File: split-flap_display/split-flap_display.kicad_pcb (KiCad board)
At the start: 2 copper layers, 190 x 133.9 mm, 5 parts, among them U1 MIC59P60, U2 ESP-12, U3 MIC59P60, U4 MIC59P60, U5 74LS597

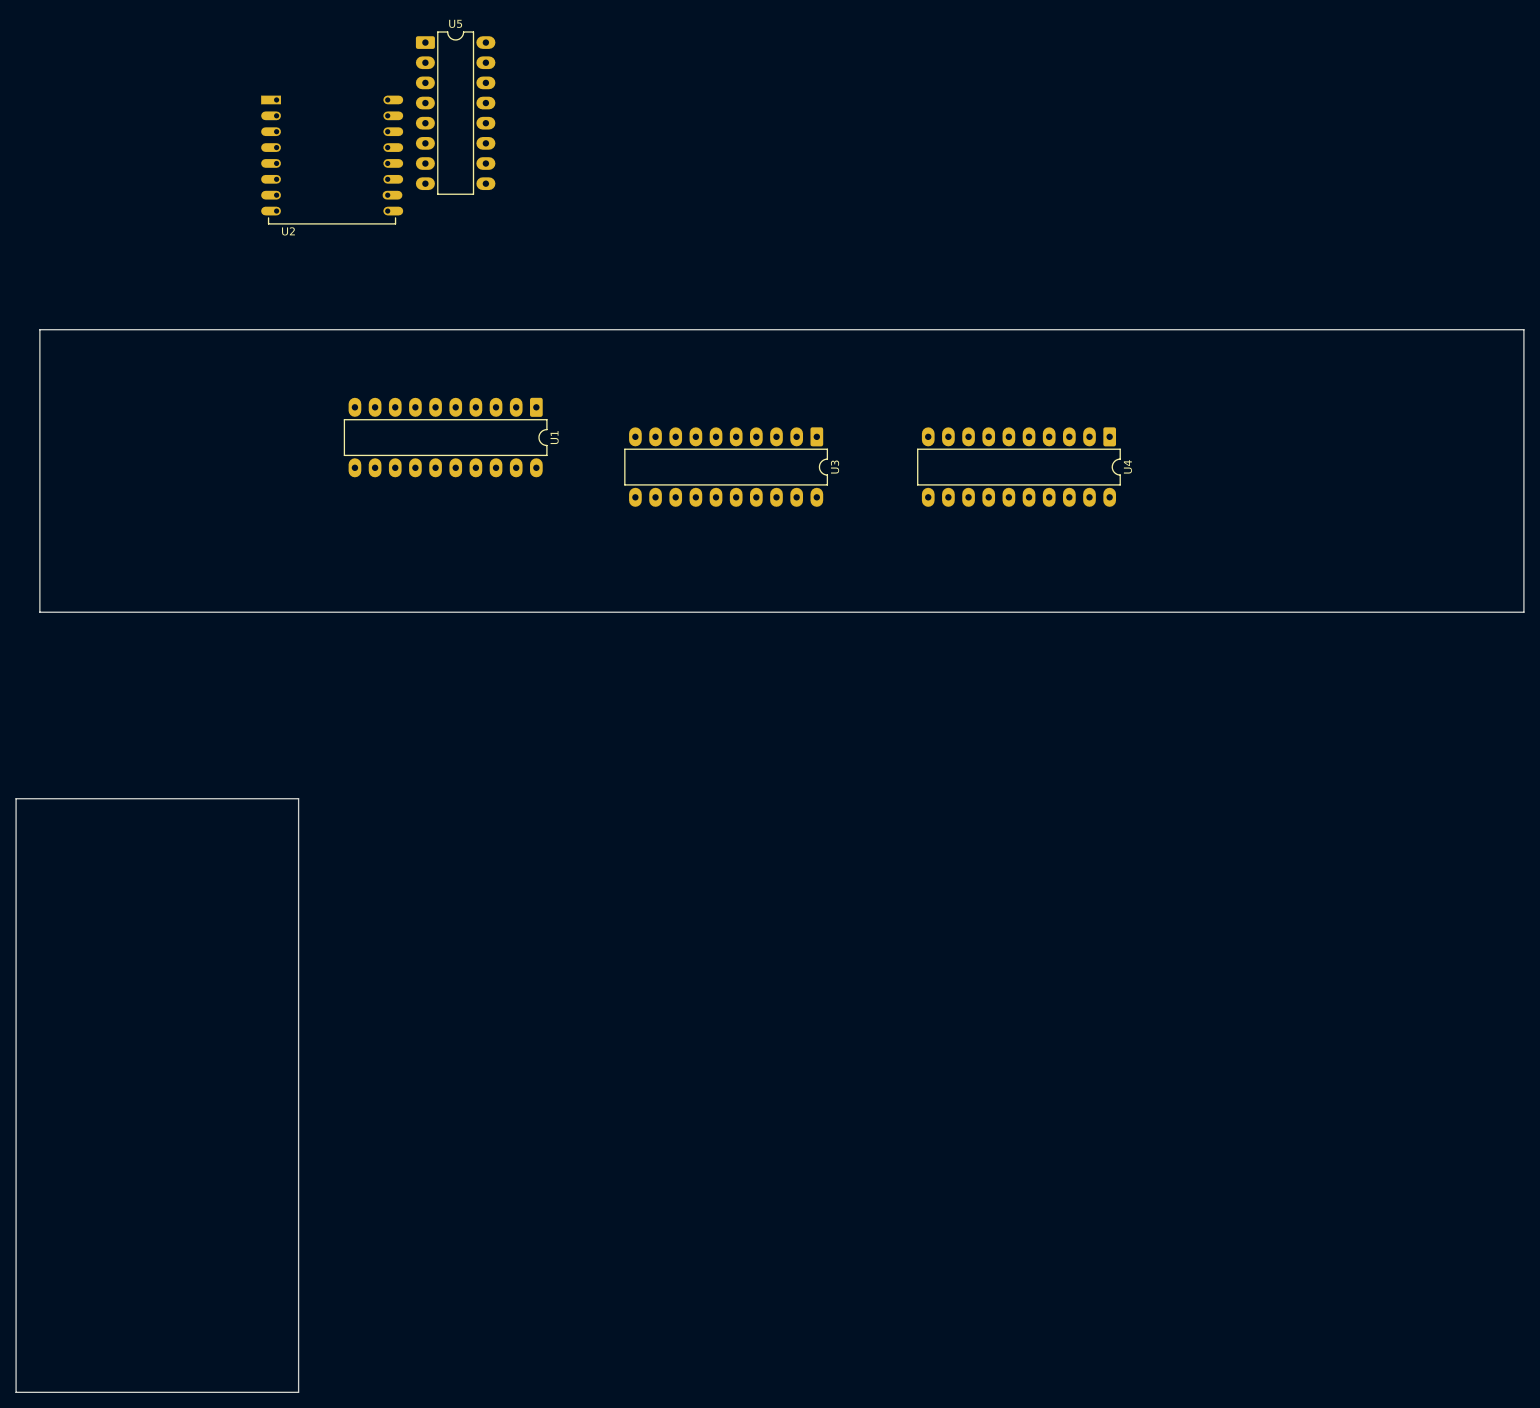
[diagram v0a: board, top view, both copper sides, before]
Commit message: added split flap source files & assembly
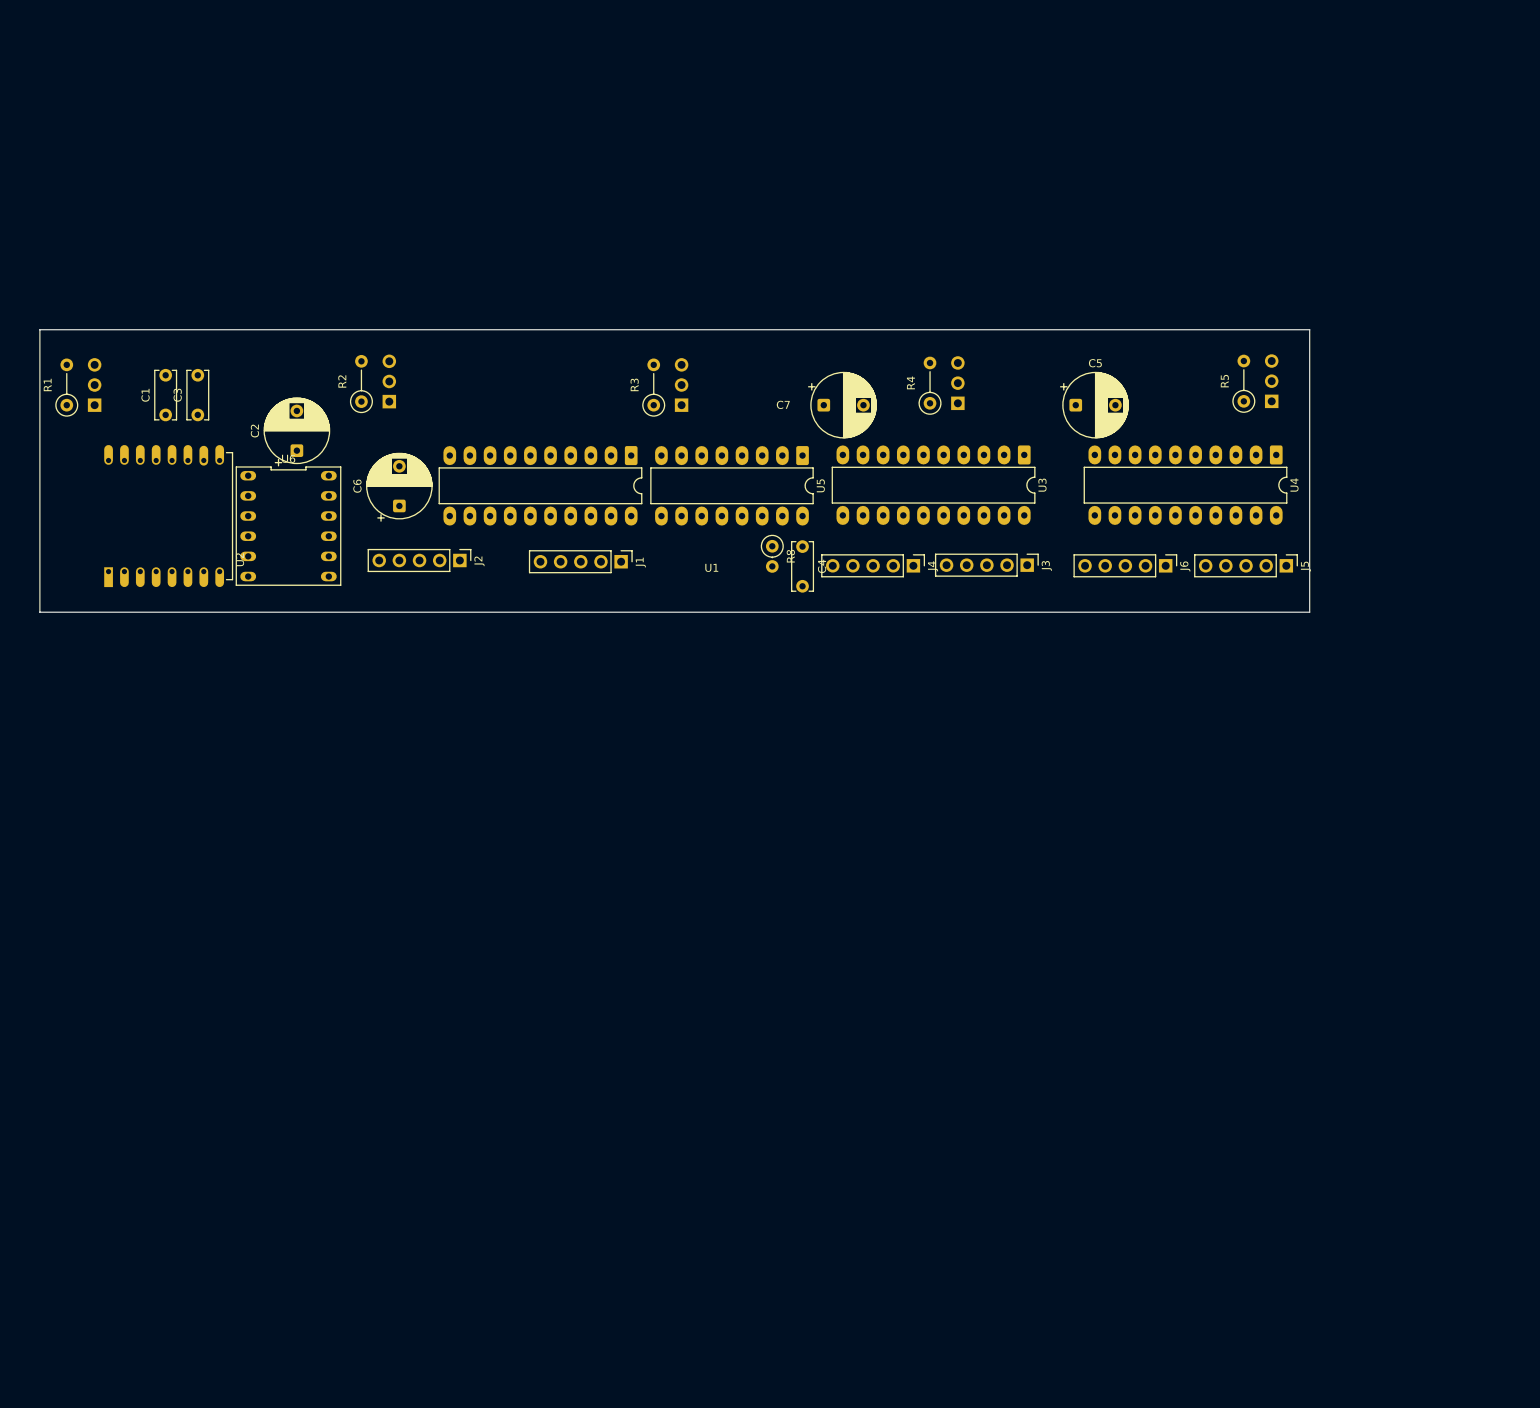
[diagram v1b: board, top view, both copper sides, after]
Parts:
- added C1: 100n, Capacitor_THT:C_Disc_D6.0mm_W2.5mm_P5.00mm, F.Cu at (72.2, 68.5)
- added C2: 100u, Capacitor_THT:CP_Radial_D8.0mm_P5.00mm, F.Cu at (88.7, 73.0)
- added C3: 100n, Capacitor_THT:C_Disc_D6.0mm_W2.5mm_P5.00mm, F.Cu at (76.2, 68.5)
- added C4: 100n, Capacitor_THT:C_Disc_D6.0mm_W2.5mm_P5.00mm, F.Cu at (152.4, 85.1)
- added C5: 100u, Capacitor_THT:CP_Radial_D8.0mm_P5.00mm, F.Cu at (186.8, 67.3)
- added C6: 100u, Capacitor_THT:CP_Radial_D8.0mm_P5.00mm, F.Cu at (101.6, 80.0)
- added C7: 100u, Capacitor_THT:CP_Radial_D8.0mm_P5.00mm, F.Cu at (155.1, 67.3)
- added J1: A, Connector_PinHeader_2.54mm:PinHeader_1x05_P2.54mm_Vertical, F.Cu at (129.5, 87.0)
- added J10: Hall4, Connector_PinHeader_2.54mm:PinHeader_1x03_P2.54mm_Vertical, B.Cu at (172.0, 67.1)
- added J11: Hall5, Connector_PinHeader_2.54mm:PinHeader_1x03_P2.54mm_Vertical, B.Cu at (211.5, 66.8)
- added J2: B, Connector_PinHeader_2.54mm:PinHeader_1x05_P2.54mm_Vertical, F.Cu at (109.2, 86.9)
- added J3: C, Connector_PinHeader_2.54mm:PinHeader_1x05_P2.54mm_Vertical, F.Cu at (180.7, 87.5)
- added J4: D, Connector_PinHeader_2.54mm:PinHeader_1x05_P2.54mm_Vertical, F.Cu at (166.4, 87.5)
- added J5: E, Connector_PinHeader_2.54mm:PinHeader_1x05_P2.54mm_Vertical, F.Cu at (213.4, 87.5)
- added J6: F, Connector_PinHeader_2.54mm:PinHeader_1x05_P2.54mm_Vertical, F.Cu at (198.2, 87.5)
- added J7: Hall1, Connector_PinHeader_2.54mm:PinHeader_1x03_P2.54mm_Vertical, B.Cu at (63.2, 67.3)
- added J8: Hall2, Connector_PinHeader_2.54mm:PinHeader_1x03_P2.54mm_Vertical, B.Cu at (100.3, 66.9)
- added J9: Hall3, Connector_PinHeader_2.54mm:PinHeader_1x03_P2.54mm_Vertical, B.Cu at (137.2, 67.3)
- added R1: 10k, Resistor_THT:R_Axial_DIN0207_L6.3mm_D2.5mm_P5.08mm_Vertical, F.Cu at (59.7, 67.3)
- added R2: 10k, Resistor_THT:R_Axial_DIN0207_L6.3mm_D2.5mm_P5.08mm_Vertical, F.Cu at (96.8, 66.9)
- added R3: 10k, Resistor_THT:R_Axial_DIN0207_L6.3mm_D2.5mm_P5.08mm_Vertical, F.Cu at (133.7, 67.3)
- added R4: 10k, Resistor_THT:R_Axial_DIN0207_L6.3mm_D2.5mm_P5.08mm_Vertical, F.Cu at (168.5, 67.1)
- added R5: 10k, Resistor_THT:R_Axial_DIN0207_L6.3mm_D2.5mm_P5.08mm_Vertical, F.Cu at (208.0, 66.8)
- added R8: 10k, Resistor_THT:R_Axial_DIN0207_L6.3mm_D2.5mm_P2.54mm_Vertical, F.Cu at (148.6, 85.1)
- added U6: LevelShifter_4ch, footprints:DIP-12_LevelShifter, F.Cu at (87.6, 82.5)
- moved U5 70.5 mm to (152.4, 73.7), turned to -90 degrees
- moved U2 63.1 mm to (65.0, 88.3), turned to 90 degrees
- moved U3 26.2 mm to (180.3, 73.6)
- moved U4 21.1 mm to (212.1, 73.6)
- moved U1 13.4 mm to (130.8, 73.7)
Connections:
- U1 pad 4: /D1 -> /Dm1
- U1 pad 7: /D2 -> /Dm2
- U2 pad 1: unconnected-(U2-REST-Pad1) -> +3.3V
- U2 pad 3: unconnected-(U2-CH_PD-Pad3) -> +3.3V
- U2 pad 4: unconnected-(U2-GPIO16-Pad4) -> /~{CS}_3v3
- U2 pad 5: unconnected-(U2-GPIO14-Pad5) -> /CLK_3v3
- U2 pad 6: unconnected-(U2-GPIO12-Pad6) -> /Dm_3v3
- U2 pad 7: /DOUT -> /Dhout_3v3
- U3 pad 4: /D2 -> /Dm2
- U3 pad 7: /D3 -> /Dm3
- U4 pad 4: /D3 -> /Dm3
- U4 pad 7: /D4 -> /Dm4
- U5 pad 1: /Hall1 -> /Hall4
- U5 pad 11: unconnected-(U5-SCK-Pad11) -> /CLK
- U5 pad 14: /D4 -> /DHin
- U5 pad 15: /Hall0 -> GND
- U5 pad 2: /Hall2 -> /Hall3
- U5 pad 3: /Hall3 -> /Hall2
- U5 pad 4: /Hall4 -> /Hall1
- U5 pad 5: /Hall5 -> /Hall0
- U5 pad 6: /Hall6 -> GND
- U5 pad 7: /Hall7 -> GND
- U5 pad 9: /D5 -> /Dhout
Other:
- board size 190 x 133.9 mm -> 160 x 35.6 mm
